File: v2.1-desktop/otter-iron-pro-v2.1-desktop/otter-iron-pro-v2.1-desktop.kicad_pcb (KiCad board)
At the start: 2 copper layers, 72 parts, among them J1 C167321, J2 +24V, J3 GND, J4 SSD1306, J5 OLED_64x32, J6 SWD, J7 C245, J8 +24V, J9 GND, Q1 SS8050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

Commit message: Layout draft
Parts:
- added C24: 0.1μF, Capacitor_SMD:C_0603_1608Metric, F.Cu at (203.8, 89.0)
- C20: footprint Capacitor_SMD:CP_Elec_10x10.5 -> Capacitor_THT:CP_Radial_D12.5mm_P5.00mm; moved to B.Cu
- C23: footprint Capacitor_SMD:CP_Elec_10x10.5 -> Capacitor_THT:CP_Radial_D8.0mm_P3.50mm
- SW1, SW2: footprint Button_Switch_SMD:SW_SPST_EVQP7C -> Button_Switch_THT:SW_PUSH_6mm_H13mm
- moved J6 74.7 mm to (202.8, 99.5)
- moved C6 73.0 mm to (157.8, 103.2), turned to 180 degrees
- moved R2 70.9 mm to (157.8, 101.8), turned to 180 degrees
- moved J5 66.3 mm to (161.5, 99.5), turned to 270 degrees
- moved C8 65.9 mm to (157.8, 104.8), turned to 180 degrees
- moved C23 65.1 mm to (195.8, 83.8), turned to 270 degrees
- moved SW2 59.9 mm to (208.5, 95.2), turned to 180 degrees
- moved L1 53.7 mm to (188.0, 89.0)
- moved NT1 53.5 mm to (203.5, 73.7), turned to 90 degrees
- moved SW1 52.7 mm to (202.0, 103.8)
- moved J4 52.5 mm to (181.8, 83.8)
- moved R15 51.4 mm to (200.2, 88.5), turned to 180 degrees
- moved U7 48.3 mm to (192.8, 107.2), turned to 270 degrees
- moved R19 46.2 mm to (168.0, 87.0)
- moved R20 42.8 mm to (199.5, 86.2), turned to 270 degrees
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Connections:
- C1 pad 1: VBUS -> VCC
- F1 pad 1: VBUS -> VCC
- F1 pad 2: Net-(F1-Pad2) -> VBUS
- J2 pad 1: Net-(F1-Pad2) -> VBUS
- J8 pad 1: Net-(F1-Pad2) -> VBUS
- R13 pad 1: VBUS -> VCC
- R17 pad 1: VBUS -> VCC
- R19 pad 1: VBUS -> VCC
- U1 pad 1: VBUS -> VCC
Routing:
- net +3V3: track 0.00 -> 155.4 mm, vias 0 -> 4
- net GND: track 0.00 -> 109.6 mm, vias 0 -> 24
- net VBUS: track 0.00 -> 69.7 mm
- net VCC: track 0.00 -> 45.8 mm
- net OLED_SCL: track 0.00 -> 39.8 mm, vias 0 -> 5
- net OLED_SDA: track 0.00 -> 39.5 mm, vias 0 -> 5
- net PWM: track 0.00 -> 38.4 mm, vias 0 -> 8
- net INT_N: track 0.00 -> 37.4 mm, vias 0 -> 4
- net SW1: track 0.00 -> 37.3 mm, vias 0 -> 2
- net SW2: track 0.00 -> 30.9 mm, vias 0 -> 2
- net TTIP: track 0.00 -> 29.8 mm, vias 0 -> 2
- net IIN: track 0.00 -> 20.0 mm
- net Net-(C21-Pad1): track 0.00 -> 19.6 mm
- net CC2: track 0.00 -> 19.3 mm, vias 0 -> 2
- net C245_JUNC: track 0.00 -> 15.1 mm
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- added copper zone on B.Cu, net GND
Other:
- board outline added: 63 x 50 mm

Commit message: Finish layout
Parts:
- moved C10 1.46 mm to (181.6, 73.7)
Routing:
- net USB_N: track 6.80 -> 49.3 mm, vias 0 -> 4
- net USB_P: track 10.3 -> 49.7 mm, vias 0 -> 2
- net GND: track 109.6 -> 139.9 mm, vias 24 -> 35
- net SWDIO: track 0.00 -> 25.1 mm, vias 0 -> 2
- net +3V3: track 155.4 -> 180.0 mm, vias 4 -> 7
- net SWCLK: track 0.00 -> 21.7 mm, vias 0 -> 2
- net OLED_SCL: track 39.8 -> 60.5 mm
- net OLED_SDA: track 39.5 -> 59.6 mm, vias 5 -> 6
- net Net-(Q2-Pad2): track 3.34 -> 19.6 mm
- net Net-(C20-Pad1): track 12.7 -> 26.3 mm
- net Net-(D1-Pad1): track 0.00 -> 10.9 mm
- net SW2: track 30.9 -> 39.2 mm
- net Net-(Q4-Pad1): track 0.00 -> 4.12 mm
- net CC2: track 19.3 -> 16.8 mm
- net CC1: track 13.3 -> 11.8 mm
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
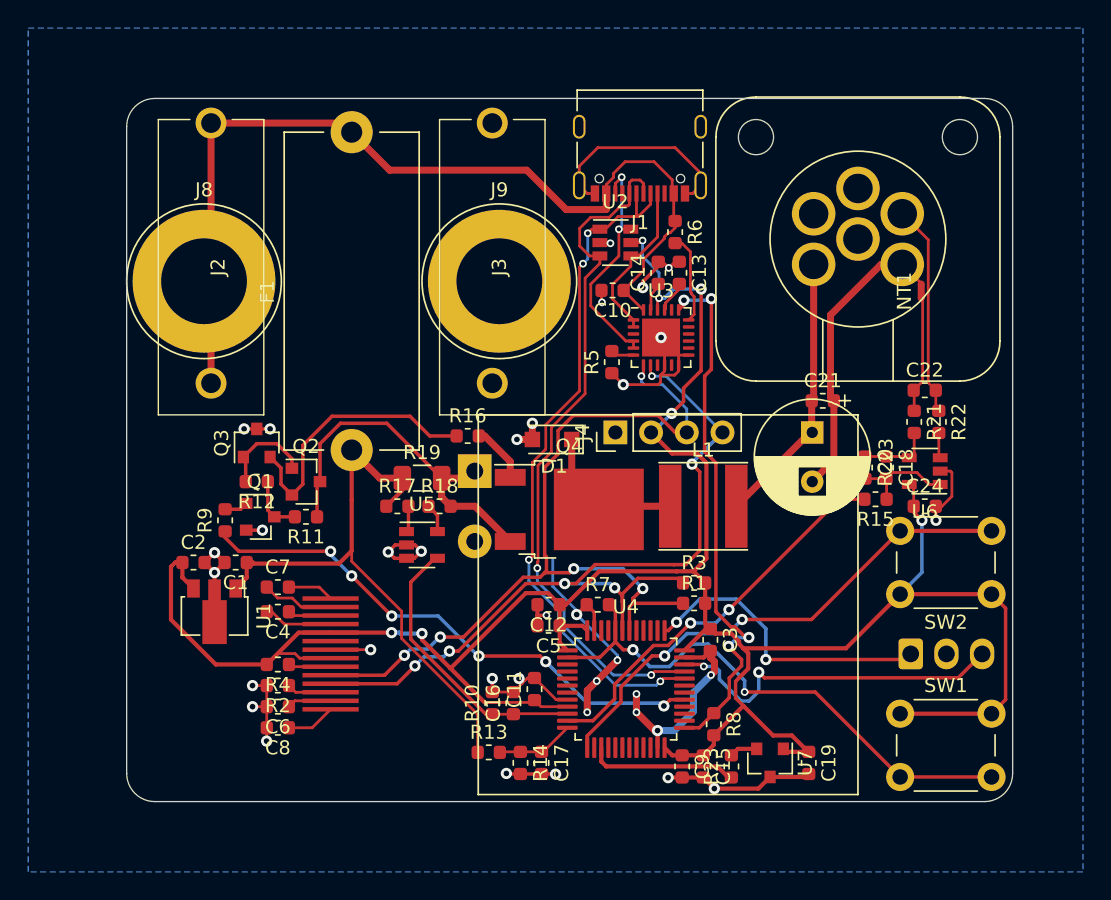
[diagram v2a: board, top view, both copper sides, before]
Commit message: Silkscreen and GND area fill
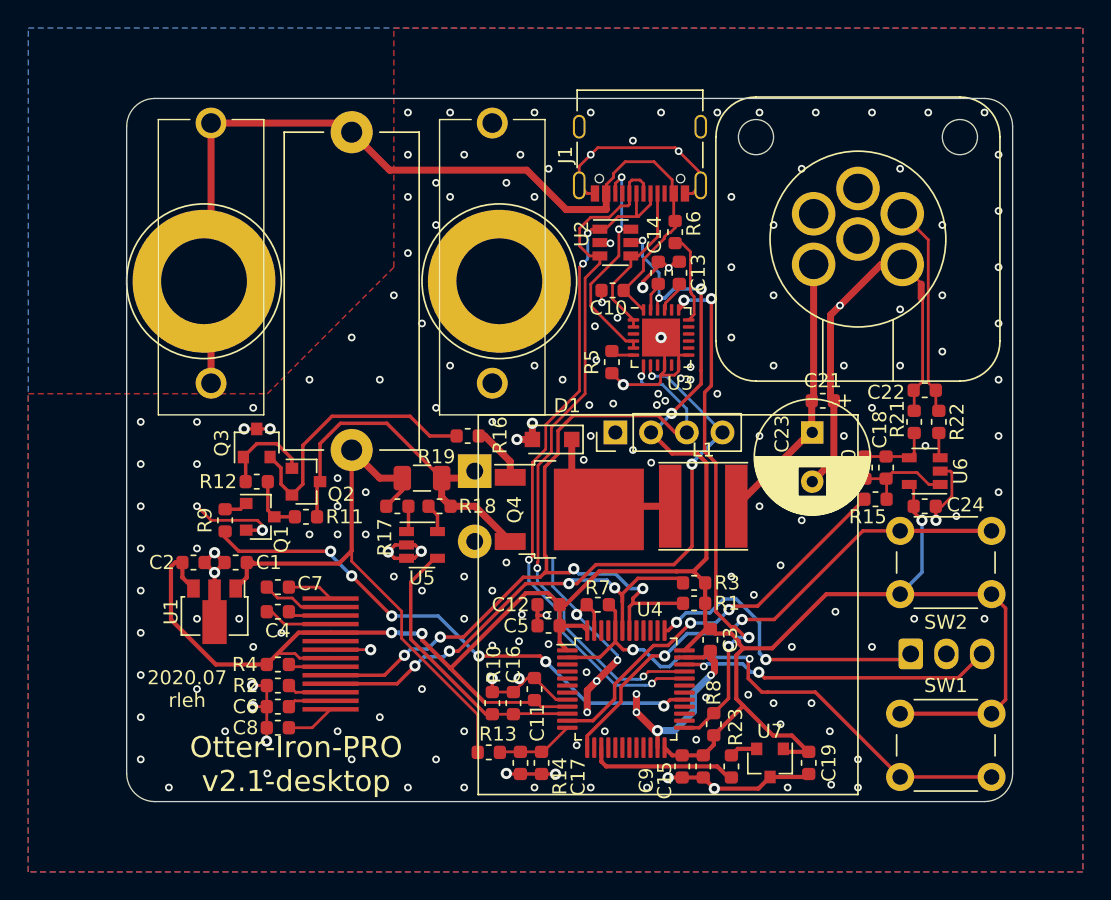
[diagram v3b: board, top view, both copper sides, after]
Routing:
- net GND: track 139.9 -> 145.4 mm, vias 35 -> 186
- net SWDIO: track 25.1 -> 22.4 mm
- net OLED_SDA: track 59.6 -> 58.6 mm
- net INT_N: track 38.9 -> 38.1 mm
- added copper zone on F.Cu, net GND
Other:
- board text added: "2020.07 rleh"
- board text added: "Otter-Iron-PRO v2.1-desktop"

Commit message: Export gerbers; Add LCSC part numbers
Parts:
- D1: value B140-E3 -> B140-E3 or MBR340F
- L1: value 4.7u -> 4.7u; e.g. SNR6045K-4R7N
- Q3: value BC807 -> BC807 or MMBT5401
- SW1: value key2 -> 6x6mm
- SW2: value key1 -> 6x6mm
- U4: value STM32F072C8Tx -> STM32F072C8T6
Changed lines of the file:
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@@
       (outputformat 1)
       (mirror false)
-      (drillshape 1)
+      (drillshape 0)
       (scaleselection 1)
-      (outputdirectory ""))
+      (outputdirectory "gerber/"))
   )
   (net 0 "")
@@
     (add_net "Net-(C8-Pad1)")
     (add_net "Net-(D1-Pad1)")
+    (add_net "Net-(J1-PadA8)")
+    (add_net "Net-(J1-PadB8)")
     (add_net "Net-(J5-Pad12)")
+    (add_net "Net-(J5-Pad6)")
     (add_net "Net-(J5-Pad9)")
+    (add_net "Net-(J7-Pad3)")
+    (add_net "Net-(J7-Pad4)")
+    (add_net "Net-(J7-Pad6)")
     (add_net "Net-(Q1-Pad1)")
     (add_net "Net-(Q1-Pad3)")
@@
     (add_net "Net-(R5-Pad2)")
     (add_net "Net-(R6-Pad2)")
+    (add_net "Net-(U3-Pad11)")
+    (add_net "Net-(U3-Pad14)")
+    (add_net "Net-(U3-Pad15)")
+    (add_net "Net-(U3-Pad16)")
+    (add_net "Net-(U3-Pad17)")
+    (add_net "Net-(U3-Pad20)")
+    (add_net "Net-(U3-Pad3)")
+    (add_net "Net-(U3-Pad9)")
+    (add_net "Net-(U4-Pad14)")
+    (add_net "Net-(U4-Pad16)")
+    (add_net "Net-(U4-Pad17)")
+    (add_net "Net-(U4-Pad18)")
+    (add_net "Net-(U4-Pad19)")
+    (add_net "Net-(U4-Pad20)")
+    (add_net "Net-(U4-Pad21)")
+    (add_net "Net-(U4-Pad22)")
+    (add_net "Net-(U4-Pad26)")
+    (add_net "Net-(U4-Pad27)")
+    (add_net "Net-(U4-Pad28)")
+    (add_net "Net-(U4-Pad3)")
+    (add_net "Net-(U4-Pad30)")
+    (add_net "Net-(U4-Pad31)")
+    (add_net "Net-(U4-Pad38)")
+    (add_net "Net-(U4-Pad39)")
+    (add_net "Net-(U4-Pad4)")
+    (add_net "Net-(U4-Pad40)")
+    (add_net "Net-(U4-Pad41)")
+    (add_net "Net-(U4-Pad45)")
+    (add_net "Net-(U4-Pad46)")
+    (add_net "Net-(U4-Pad5)")
+    (add_net "Net-(U4-Pad6)")
     (add_net OLED_SCL)
     (add_net OLED_SDA)
@@
     (add_net VBUS)
     (add_net VCC)
+    (add_net nRST)
   )
   (module Button_Switch_THT:SW_PUSH_6mm_H13mm (layer F.Cu)
@@
       (effects (font (size 1 1) (thickness 0.15)))
     )
-    (fp_text value key1 (at 3.75 6.7) (layer F.Fab)
+    (fp_text value 6x6mm (at 3.75 6.7) (layer F.Fab)
       (effects (font (size 1 1) (thickness 0.15)))
     )
@@
       (effects (font (size 1 1) (thickness 0.15)))
     )
-    (fp_text value key2 (at 3.75 6.7) (layer F.Fab)
+    (fp_text value 6x6mm (at 3.75 6.7) (layer F.Fab)
       (effects (font (size 1 1) (thickness 0.15)))
     )
@@
       (effects (font (size 1 1) (thickness 0.15)))
     )
-    (fp_text value STM32F072C8Tx (at 0 5.85) (layer F.Fab)
+    (fp_text value STM32F072C8T6 (at 0 5.85) (layer F.Fab)
       (effects (font (size 1 1) (thickness 0.15)))
     )
@@
       (effects (font (size 1 1) (thickness 0.15)))
     )
-    (fp_text value BC807 (at 0 2.5 90) (layer F.Fab)
+    (fp_text value "BC807 or MMBT5401" (at 0 2.5 90) (layer F.Fab)
       (effects (font (size 1 1) (thickness 0.15)))
     )
@@
       (effects (font (size 1 1) (thickness 0.15)))
     )
-    (fp_text value 4.7u (at 0 4.5) (layer F.Fab)
+    (fp_text value "4.7u; e.g. SNR6045K-4R7N" (at 0 4.5) (layer F.Fab)
       (effects (font (size 1 1) (thickness 0.15)))
     )
@@
       (effects (font (size 1 1) (thickness 0.15)))
     )
-    (fp_text value B140-E3 (at 0 2.1) (layer F.Fab)
-      (effects (font (size 1 1) (thickness 0.15)))
-    )
+    (fp_text value "B140-E3 or MBR340F" (at 0 2.1) (layer F.Fab)
+      (effects (font (size 1 1) (thickness 0.15)))
+    )
